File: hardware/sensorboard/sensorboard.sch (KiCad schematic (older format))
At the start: 15 parts, among them P1 PWR, P2 PROG, U1 ESP-07v2, U2 TC1262, U3 BMP180_board, U4 DHT22

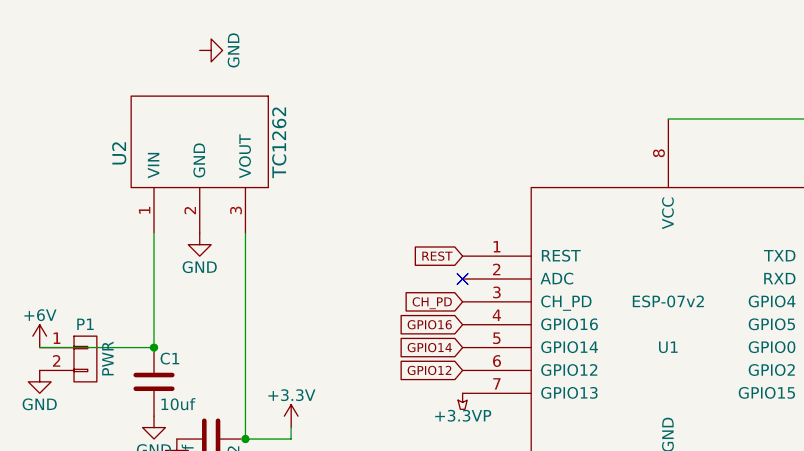
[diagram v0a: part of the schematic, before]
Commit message: Measure the actual battery voltage on ADC pin.
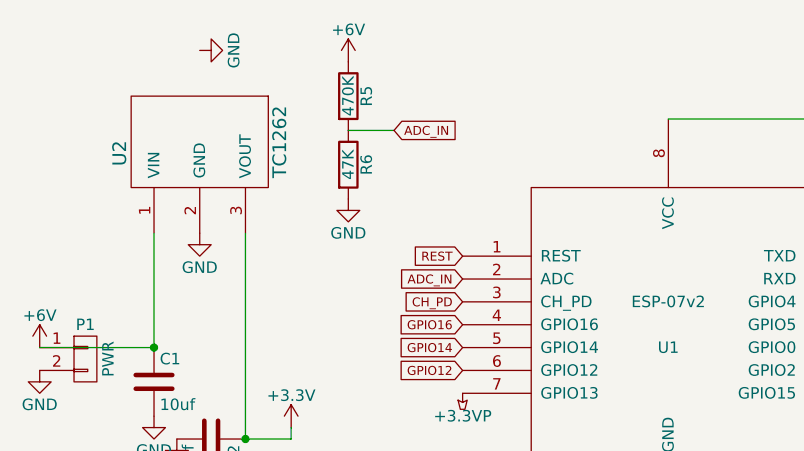
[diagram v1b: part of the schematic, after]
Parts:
- added R5: 470K, symbol R
- added R6: 47K, symbol R
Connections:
- net +6V: now also R5.1
- net GND: now also R6.2
- net ADC_IN: now reaches U1.2 (ADC)
- net ADC_IN: now also R5.2, R6.1
- no-connect marks 3 -> 2
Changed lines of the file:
@@
 Text GLabel 2450 1500 0    39   Input ~ 0
 REST
-NoConn ~ 2450 1600
 $Comp
 L BMP180_board U3
@@
 	0    -1   -1   0
 $EndComp
+Text GLabel 2450 1600 0    39   Input ~ 0
+ADC_IN
+Text GLabel 2150 950  2    39   Input ~ 0
+ADC_IN
+$Comp
+L GND #PWR?
+U 1 1 562D40D4
+P 1950 1250
+F 0 "#PWR?" H 1950 1000 50  0001 C CNN
+F 1 "GND" H 1950 1100 50  0000 C CNN
+F 2 "" H 1950 1250 60  0000 C CNN
+F 3 "" H 1950 1250 60  0000 C CNN
+	1    1950 1250
+	1    0    0    -1
+$EndComp
+$Comp
+L +6V #PWR?
+U 1 1 562D410C
+P 1950 650
+F 0 "#PWR?" H 1950 500 50  0001 C CNN
+F 1 "+6V" H 1950 790 50  0000 C CNN
+F 2 "" H 1950 650 60  0000 C CNN
+F 3 "" H 1950 650 60  0000 C CNN
+	1    1950 650
+	1    0    0    -1
+$EndComp
+$Comp
+L R R5
+U 1 1 562D41A2
+P 1950 800
+F 0 "R5" V 2030 800 50  0000 C CNN
+F 1 "470K" V 1950 800 50  0000 C CNN
+F 2 "" V 1880 800 30  0000 C CNN
+F 3 "" H 1950 800 30  0000 C CNN
+	1    1950 800
+	1    0    0    -1
+$EndComp
+$Comp
+L R R6
+U 1 1 562D41F0
+P 1950 1100
+F 0 "R6" V 2030 1100 50  0000 C CNN
+F 1 "47K" V 1950 1100 50  0000 C CNN
+F 2 "" V 1880 1100 30  0000 C CNN
+F 3 "" H 1950 1100 30  0000 C CNN
+	1    1950 1100
+	1    0    0    -1
+$EndComp
+Wire Wire Line
+	1950 950  2150 950
 $EndSCHEMATC

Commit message: Change some footprints.
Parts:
- C3, C4, C5: footprint Capacitors_SMD:C_0805_HandSoldering -> Capacitors_SMD:C_0603_HandSoldering
- R1, R2, R3, R4: footprint Resistors_SMD:R_1206_HandSoldering -> Resistors_SMD:R_0603_HandSoldering
- R5, R6: footprint (none) -> Resistors_SMD:R_0603_HandSoldering
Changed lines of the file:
@@
 F 0 "C3" H 4525 1150 50  0000 L CNN
 F 1 "100nf" H 4525 950 50  0000 L CNN
-F 2 "Capacitors_SMD:C_0805_HandSoldering" H 4538 900 30  0001 C CNN
+F 2 "Capacitors_SMD:C_0603_HandSoldering" H 4538 900 30  0001 C CNN
 F 3 "" H 4500 1050 60  0000 C CNN
 	1    4500 1050
@@
 F 0 "C4" H 925 3700 50  0000 L CNN
 F 1 "100nf" H 925 3500 50  0000 L CNN
-F 2 "Capacitors_SMD:C_0805_HandSoldering" H 938 3450 30  0001 C CNN
+F 2 "Capacitors_SMD:C_0603_HandSoldering" H 938 3450 30  0001 C CNN
 F 3 "" H 900 3600 60  0000 C CNN
 	1    900  3600
@@
 F 0 "C5" H 2025 3750 50  0000 L CNN
 F 1 "100nf" H 2025 3550 50  0000 L CNN
-F 2 "Capacitors_SMD:C_0805_HandSoldering" H 2038 3500 30  0001 C CNN
+F 2 "Capacitors_SMD:C_0603_HandSoldering" H 2038 3500 30  0001 C CNN
 F 3 "" H 2000 3650 60  0000 C CNN
 	1    2000 3650
@@
 F 0 "R1" V 3130 3350 50  0000 C CNN
 F 1 "10k" V 3050 3350 50  0000 C CNN
-F 2 "Resistors_SMD:R_1206_HandSoldering" V 2980 3350 30  0001 C CNN
+F 2 "Resistors_SMD:R_0603_HandSoldering" V 2980 3350 30  0001 C CNN
 F 3 "" H 3050 3350 30  0000 C CNN
 	1    3050 3350
@@
 F 0 "R2" V 3380 3500 50  0000 C CNN
 F 1 "10k" V 3300 3500 50  0000 C CNN
-F 2 "Resistors_SMD:R_1206_HandSoldering" V 3230 3500 30  0001 C CNN
+F 2 "Resistors_SMD:R_0603_HandSoldering" V 3230 3500 30  0001 C CNN
 F 3 "" H 3300 3500 30  0000 C CNN
 	1    3300 3500
@@
 F 0 "R3" V 5330 3050 50  0000 C CNN
 F 1 "10k" V 5250 3050 50  0000 C CNN
-F 2 "Resistors_SMD:R_1206_HandSoldering" V 5180 3050 30  0001 C CNN
+F 2 "Resistors_SMD:R_0603_HandSoldering" V 5180 3050 30  0001 C CNN
 F 3 "" H 5250 3050 30  0000 C CNN
 	1    5250 3050
@@
 F 0 "R4" V 5780 3050 50  0000 C CNN
 F 1 "10k" V 5700 3050 50  0000 C CNN
-F 2 "Resistors_SMD:R_1206_HandSoldering" V 5630 3050 30  0001 C CNN
+F 2 "Resistors_SMD:R_0603_HandSoldering" V 5630 3050 30  0001 C CNN
 F 3 "" H 5700 3050 30  0000 C CNN
 	1    5700 3050
@@
 ADC_IN
 $Comp
-L GND #PWR?
+L GND #PWR022
 U 1 1 562D40D4
 P 1950 1250
-F 0 "#PWR?" H 1950 1000 50  0001 C CNN
+F 0 "#PWR022" H 1950 1000 50  0001 C CNN
 F 1 "GND" H 1950 1100 50  0000 C CNN
 F 2 "" H 1950 1250 60  0000 C CNN
@@
 $EndComp
 $Comp
-L +6V #PWR?
+L +6V #PWR023
 U 1 1 562D410C
 P 1950 650
-F 0 "#PWR?" H 1950 500 50  0001 C CNN
+F 0 "#PWR023" H 1950 500 50  0001 C CNN
 F 1 "+6V" H 1950 790 50  0000 C CNN
 F 2 "" H 1950 650 60  0000 C CNN
@@
 F 0 "R5" V 2030 800 50  0000 C CNN
 F 1 "470K" V 1950 800 50  0000 C CNN
-F 2 "" V 1880 800 30  0000 C CNN
+F 2 "Resistors_SMD:R_0603_HandSoldering" V 1880 800 30  0001 C CNN
 F 3 "" H 1950 800 30  0000 C CNN
 	1    1950 800
@@
 F 0 "R6" V 2030 1100 50  0000 C CNN
 F 1 "47K" V 1950 1100 50  0000 C CNN
-F 2 "" V 1880 1100 30  0000 C CNN
+F 2 "Resistors_SMD:R_0603_HandSoldering" V 1880 1100 30  0001 C CNN
 F 3 "" H 1950 1100 30  0000 C CNN
 	1    1950 1100

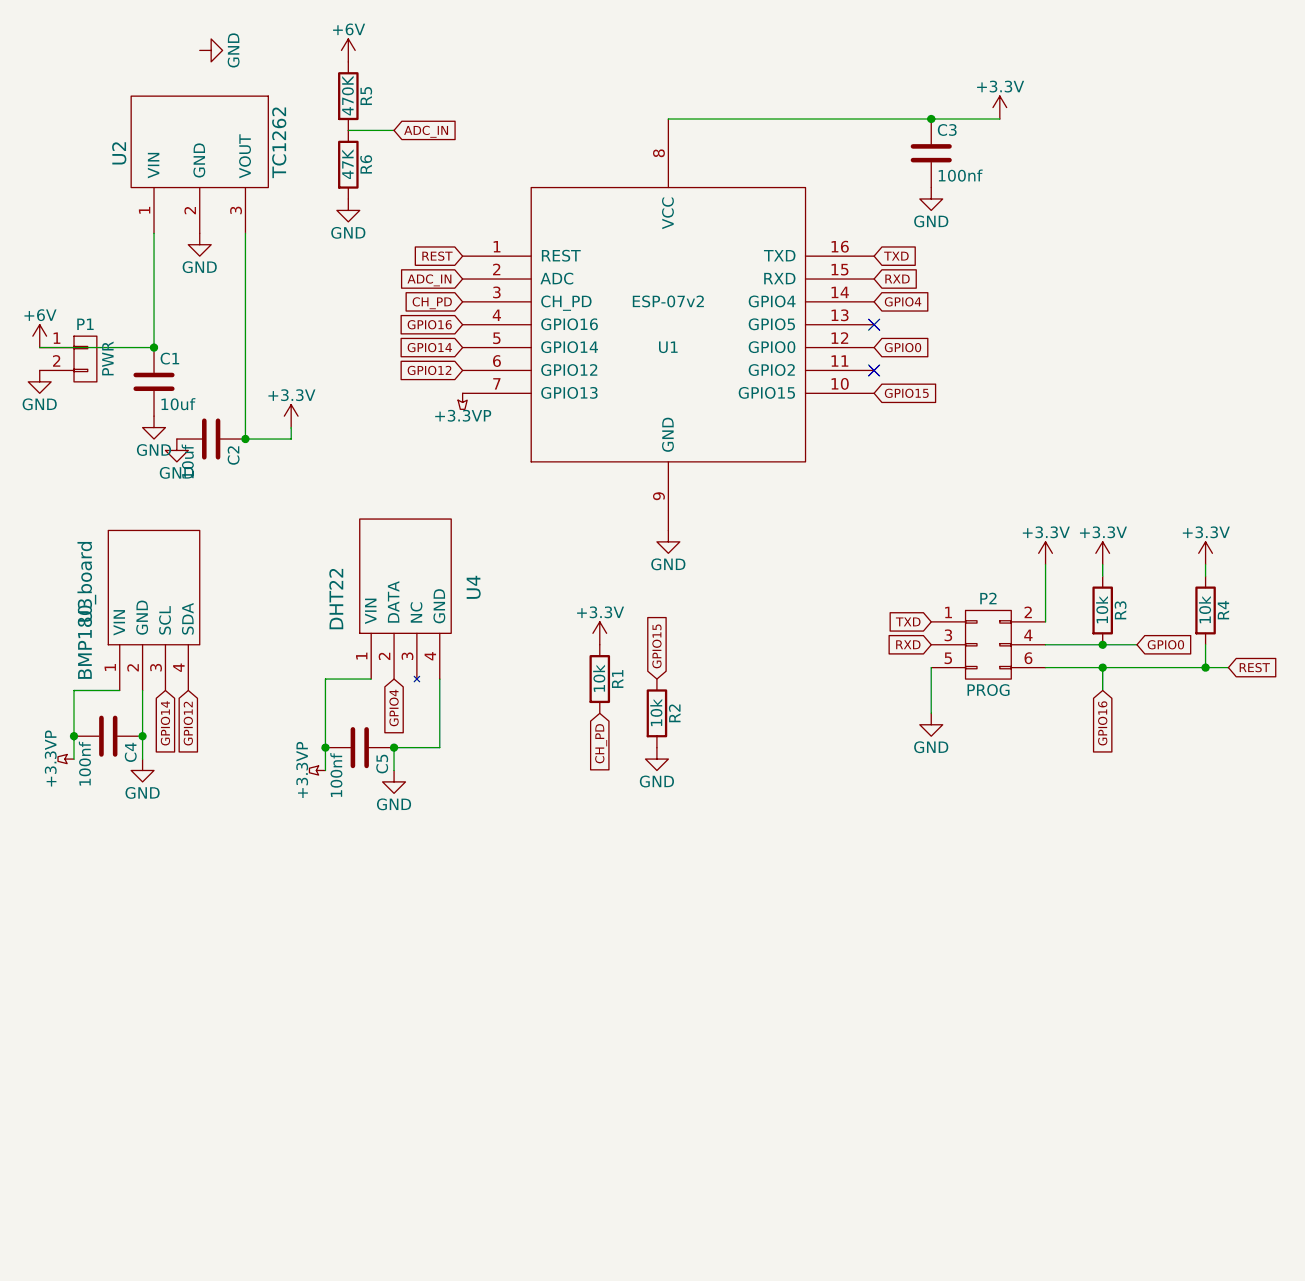
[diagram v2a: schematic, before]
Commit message: Attempt one at switching power supply.
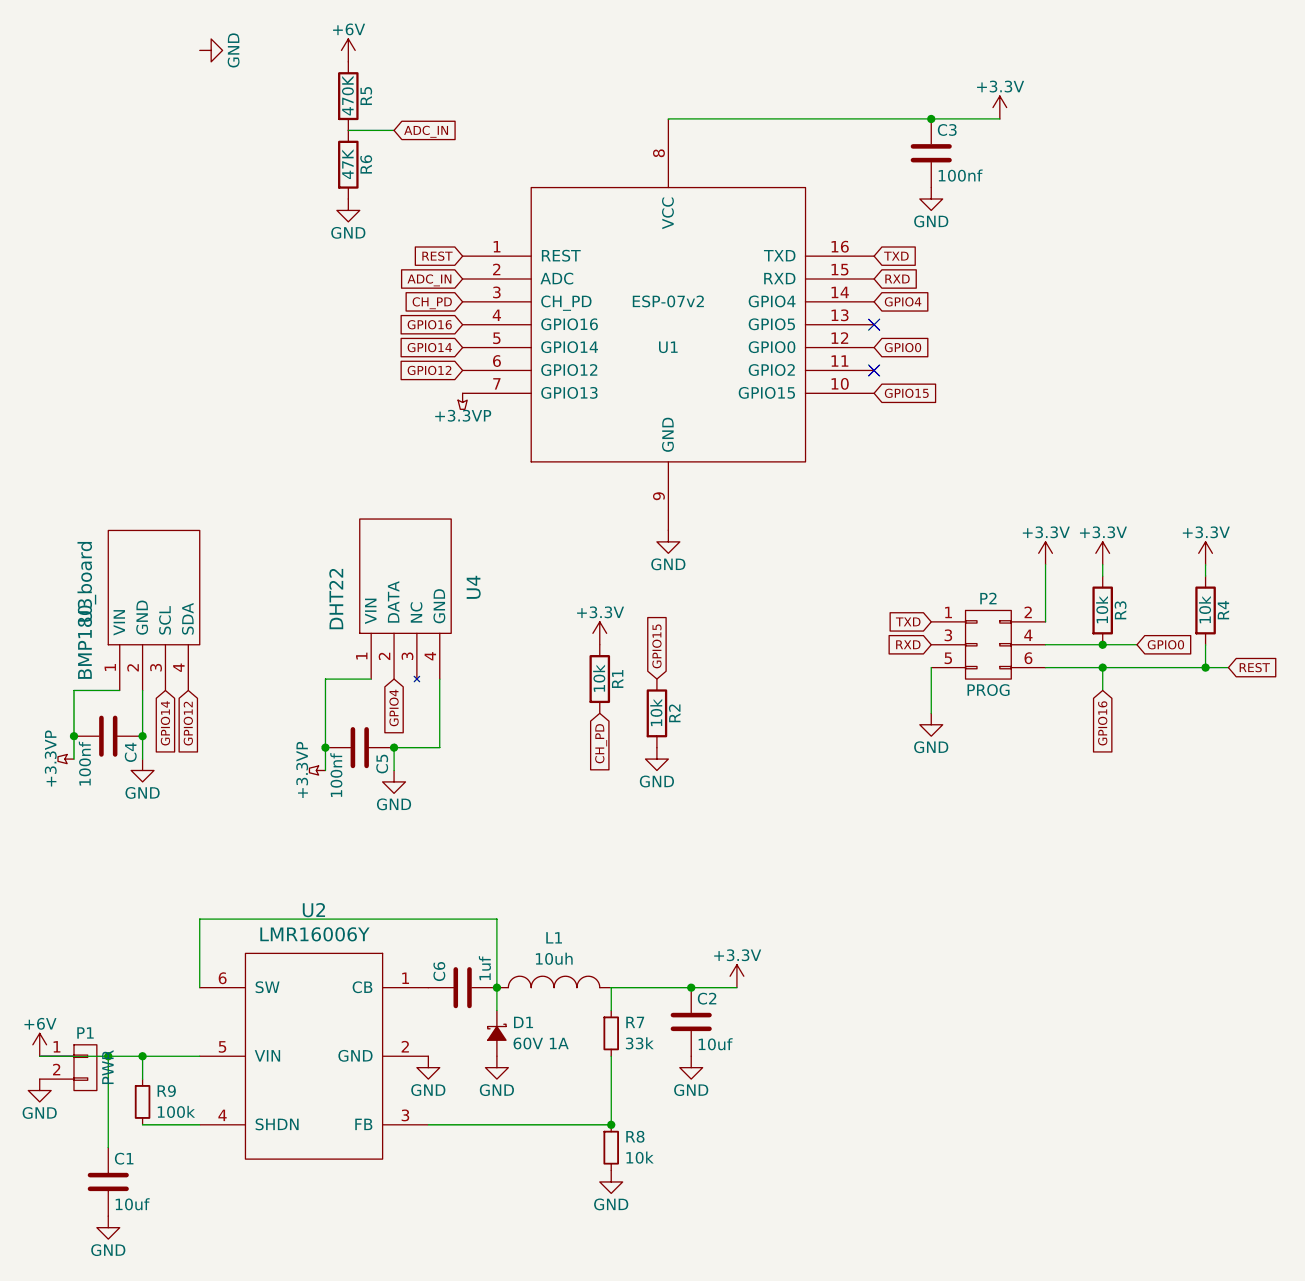
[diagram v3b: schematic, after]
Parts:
- removed U2: TC1262, TO_SOT_Packages_SMD:SOT-223, symbol TC1262
- added C6: 1uf, Capacitors_SMD:C_0603_HandSoldering, symbol C
- added D1: 60V 1A, Diodes_SMD:SOD-123, symbol D_Schottky_Small
- added L1: 10uh, Inductors:NR8040_HandSoldering, symbol INDUCTOR_SMALL
- added R7: 33k, Resistors_SMD:R_0603_HandSoldering, symbol R_Small
- added R8: 10k, Resistors_SMD:R_0603_HandSoldering, symbol R_Small
- added R9: 100k, Resistors_SMD:R_0603_HandSoldering, symbol R_Small
- added U2: LMR16006Y, TO_SOT_Packages_SMD:SOT-23-6, symbol LMR16006Y
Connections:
- net +3V3: now also L1.2, R7.1
- net +6V: now also R9.1, U2.5 (VIN)
- net GND: now also D1.2 (A), R8.2, U2.2 (GND)
- new net: C6.1, U2.1 (CB)
- new net: R7.2, R8.1, U2.3 (FB)
- new net: R9.2, U2.4 (SHDN)
- new net: C6.2, D1.1 (K), L1.1, U2.6 (SW)
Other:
- moved on the sheet: P1

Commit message: Use bme280 for sensor - initial commit
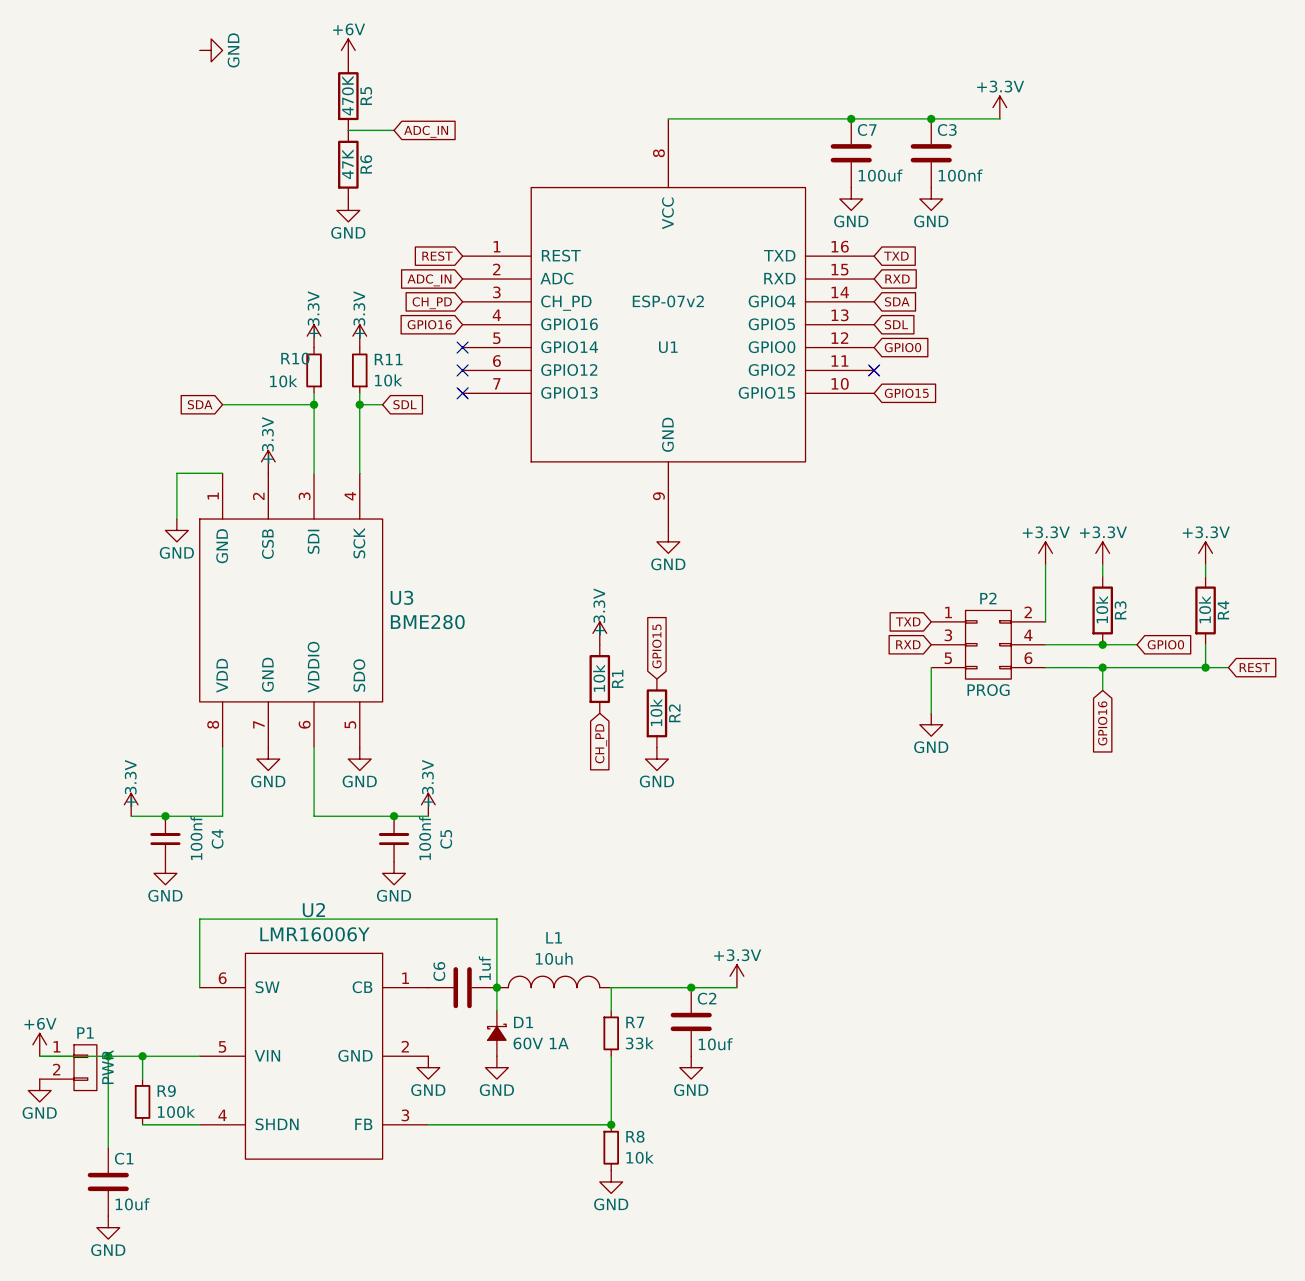
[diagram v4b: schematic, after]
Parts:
- removed C4, C5: 100nf, Capacitors_SMD:C_0603_HandSoldering, symbol C
- removed U3: BMP180_board, Pin_Headers:Pin_Header_Straight_1x04, symbol BMP180_board
- removed U4: DHT22, Pin_Headers:Pin_Header_Straight_1x04, symbol DHT22
- added C4, C5: 100nf, Capacitors_SMD:C_0603_HandSoldering, symbol C_Small
- added C7: 100uf, Capacitors_Tantalum_SMD:TantalC_SizeD_EIA-7343_HandSoldering, symbol C
- added R10, R11: 10k, Resistors_SMD:R_0603_HandSoldering, symbol R_Small
- added U3: BME280, TO_SOT_Packages_SMD:FGA8, symbol BME280
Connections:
- net +3V3: now also C4.2, C5.2, C7.1, R10.2, R11.2, U3.2 (CSB), U3.6 (VDDIO), U3.8 (VDD)
- net GND: now also C4.1, C5.1, C7.2, U3.1 (GND), U3.5 (SDO), U3.7 (GND)
- net SDL: now reaches U1.13 (GPIO5)
- net SDL: now also R11.1, U3.4 (SCK)
- net +3.3VP: no longer names the net of U1.7 (GPIO13)
- net GPIO12: no longer names the net of U1.6 (GPIO12)
- net GPIO14: no longer names the net of U1.5 (GPIO14)
- net GPIO4 renamed SDA
- net SDA: now also R10.1, U3.3 (SDI)
- no-connect marks 2 -> 4
